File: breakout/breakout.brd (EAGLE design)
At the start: 30 x 26.8 mm, 34 parts, among them X1 PCIE-MINI-CONN

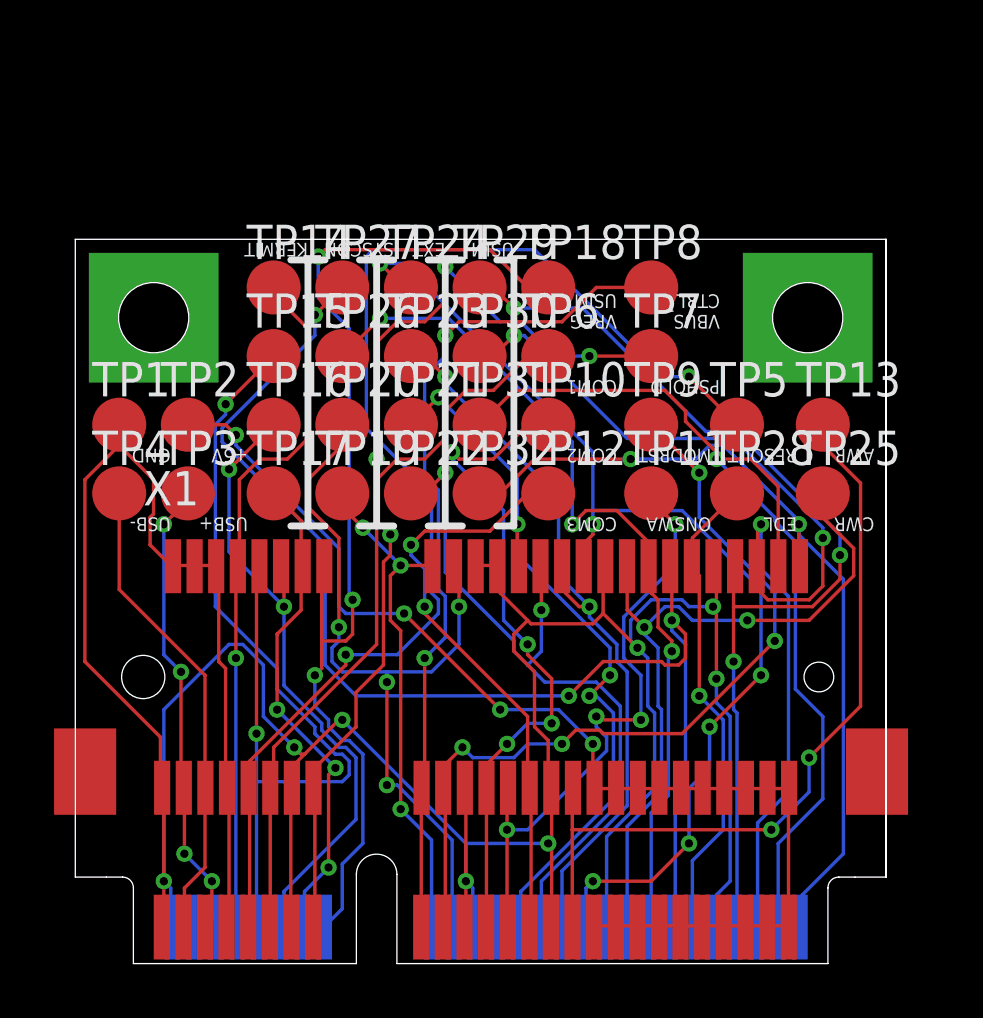
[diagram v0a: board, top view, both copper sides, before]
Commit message: Better routing of the +5V pins to handle large currents
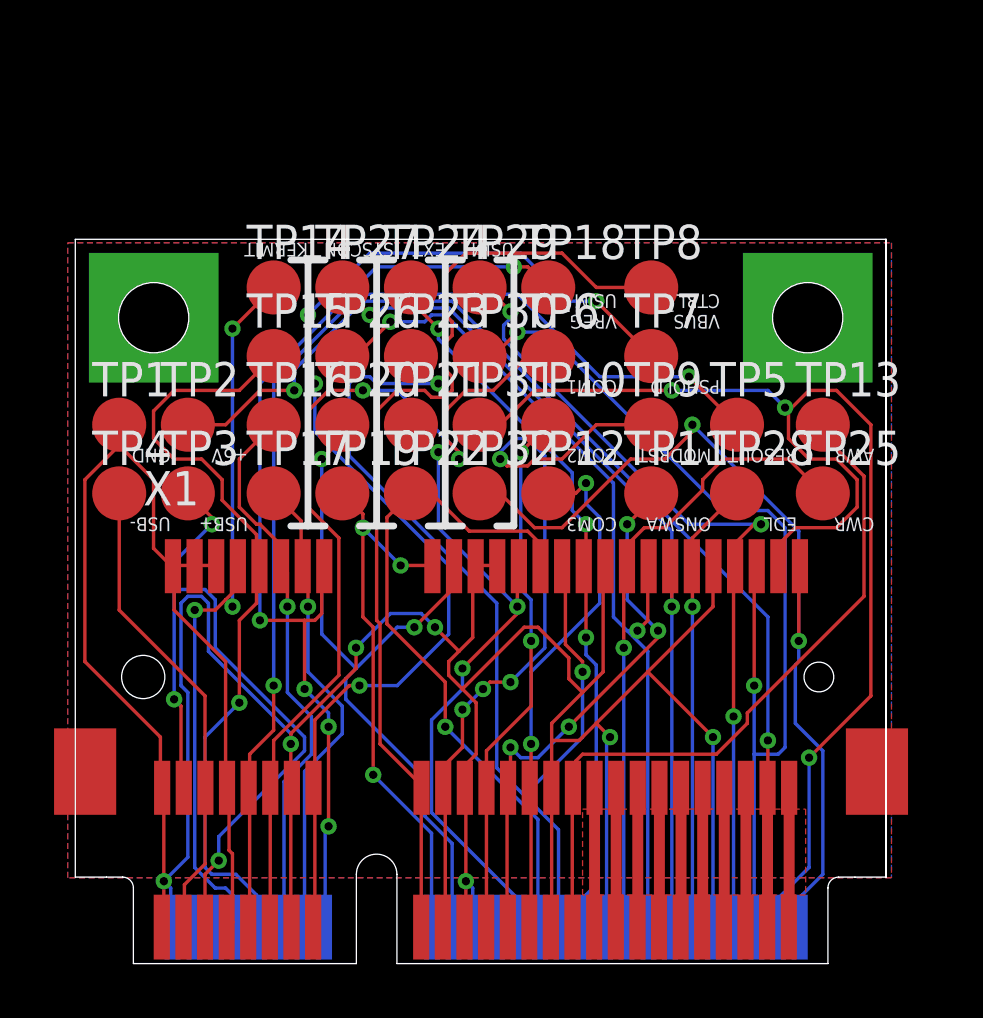
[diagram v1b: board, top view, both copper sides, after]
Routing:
- net +5V: track 43.0 -> 91.2 mm, vias 4 -> 2
- net UART_SYSCON_CTS: track 47.3 -> 32.3 mm, vias 3 -> 2
- net UART_EXT_RFR: track 40.6 -> 26.8 mm, vias 6 -> 3
- net USB_D-: track 17.3 -> 28.7 mm, vias 4 -> 3
- net UART_EXT_CTS: track 27.9 -> 38.0 mm
- net USIM_RESET_CONN: track 36.0 -> 45.7 mm, vias 1 -> 3
- net GPIO_COM1: track 27.0 -> 34.4 mm, vias 0 -> 2
- net GND: track 139.5 -> 146.8 mm, vias 8 -> 7
- net UART_KERMIT_CTS: track 35.6 -> 28.8 mm, vias 2 -> 1
- net PSHOLD: track 36.5 -> 43.2 mm
- net USIM_CLK_CONN: track 36.6 -> 30.5 mm
- net RESOUT: track 46.5 -> 41.1 mm
- net GPIO_COM2: track 24.8 -> 19.9 mm, vias 4 -> 2
- net VBUS_CTRL: track 31.2 -> 36.2 mm, vias 2 -> 0
- net CWR: track 26.9 -> 23.6 mm, vias 2 -> 1
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- added copper zone on layer 1, net +5V
- added copper zone on layer 1, net GND
- added copper zone on layer 16, net GND

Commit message: Fix incorrect signal in breakout board
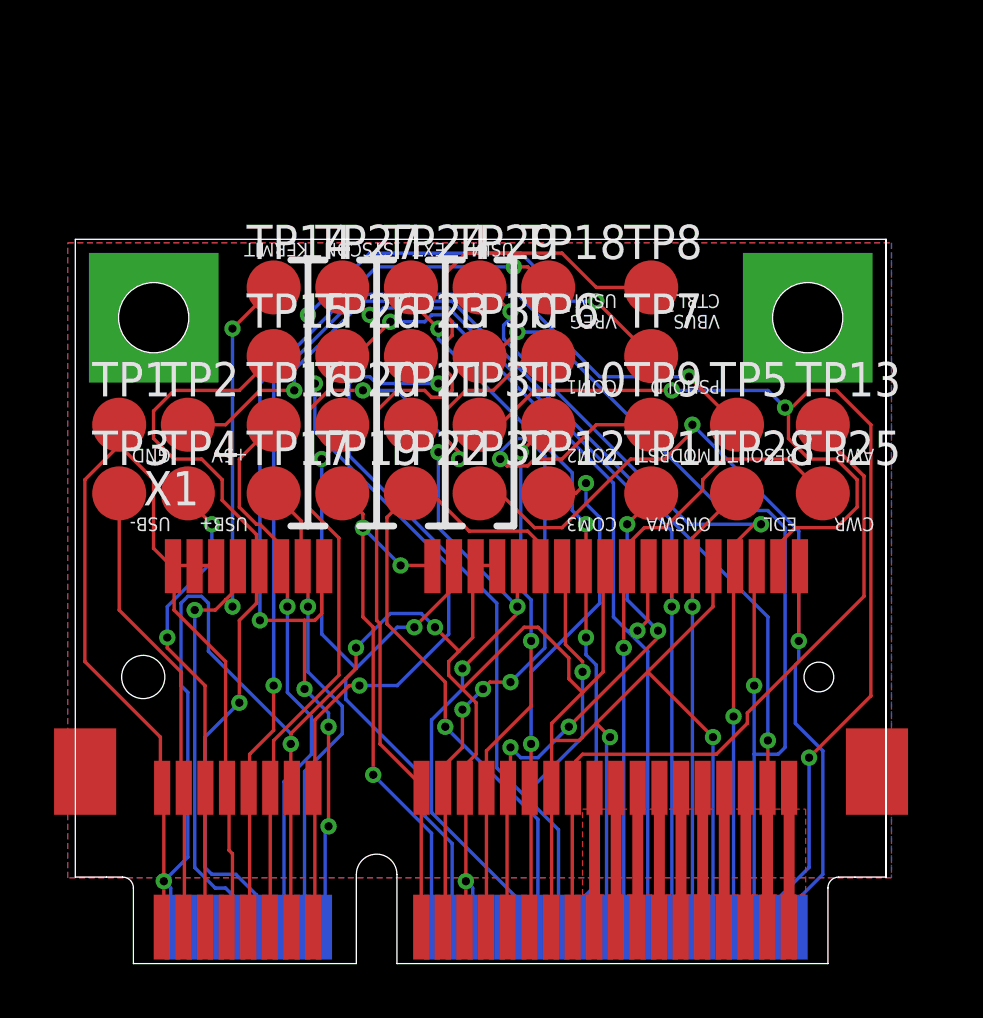
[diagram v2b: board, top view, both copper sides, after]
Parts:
- moved TP3 2.54 mm to (8.26, 22.5)
- moved TP4 2.54 mm to (10.8, 22.5)
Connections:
- removed net USB_D+: TP4.TP, U$1.3, X1.5
- removed net USB_D-: TP3.TP, U$1.5, X1.3
- new net USB_N: TP3.TP, U$1.3, X1.3
- new net USB_P: TP4.TP, U$1.5, X1.5
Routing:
- net USB_D-: track 28.7 -> 0.00 mm, vias 3 -> 0
- net USB_D+: track 17.7 -> 0.00 mm
- net USB_P: track 0.00 -> 17.7 mm, vias 0 -> 2
- net USB_N: track 0.00 -> 17.1 mm
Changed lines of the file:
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@@
 <layer number="21" name="tPlace" color="7" fill="1" visible="yes" active="yes"/>
 <layer number="22" name="bPlace" color="7" fill="1" visible="yes" active="yes"/>
-<layer number="23" name="tOrigins" color="15" fill="1" visible="no" active="yes"/>
-<layer number="24" name="bOrigins" color="15" fill="1" visible="no" active="yes"/>
-<layer number="25" name="tNames" color="7" fill="1" visible="no" active="yes"/>
-<layer number="26" name="bNames" color="7" fill="1" visible="no" active="yes"/>
-<layer number="27" name="tValues" color="7" fill="1" visible="no" active="yes"/>
-<layer number="28" name="bValues" color="7" fill="1" visible="no" active="yes"/>
+<layer number="23" name="tOrigins" color="15" fill="1" visible="yes" active="yes"/>
+<layer number="24" name="bOrigins" color="15" fill="1" visible="yes" active="yes"/>
+<layer number="25" name="tNames" color="7" fill="1" visible="yes" active="yes"/>
+<layer number="26" name="bNames" color="7" fill="1" visible="yes" active="yes"/>
+<layer number="27" name="tValues" color="7" fill="1" visible="yes" active="yes"/>
+<layer number="28" name="bValues" color="7" fill="1" visible="yes" active="yes"/>
 <layer number="29" name="tStop" color="7" fill="3" visible="no" active="yes"/>
 <layer number="30" name="bStop" color="7" fill="6" visible="no" active="yes"/>
@@
 <layer number="35" name="tGlue" color="7" fill="4" visible="no" active="yes"/>
 <layer number="36" name="bGlue" color="7" fill="5" visible="no" active="yes"/>
-<layer number="37" name="tTest" color="7" fill="1" visible="yes" active="yes"/>
-<layer number="38" name="bTest" color="7" fill="1" visible="yes" active="yes"/>
-<layer number="39" name="tKeepout" color="4" fill="11" visible="yes" active="yes"/>
-<layer number="40" name="bKeepout" color="1" fill="11" visible="yes" active="yes"/>
-<layer number="41" name="tRestrict" color="4" fill="10" visible="yes" active="yes"/>
-<layer number="42" name="bRestrict" color="1" fill="10" visible="yes" active="yes"/>
-<layer number="43" name="vRestrict" color="2" fill="10" visible="yes" active="yes"/>
+<layer number="37" name="tTest" color="7" fill="1" visible="no" active="yes"/>
+<layer number="38" name="bTest" color="7" fill="1" visible="no" active="yes"/>
+<layer number="39" name="tKeepout" color="4" fill="11" visible="no" active="yes"/>
+<layer number="40" name="bKeepout" color="1" fill="11" visible="no" active="yes"/>
+<layer number="41" name="tRestrict" color="4" fill="10" visible="no" active="yes"/>
+<layer number="42" name="bRestrict" color="1" fill="10" visible="no" active="yes"/>
+<layer number="43" name="vRestrict" color="2" fill="10" visible="no" active="yes"/>
 <layer number="44" name="Drills" color="7" fill="1" visible="yes" active="yes"/>
 <layer number="45" name="Holes" color="7" fill="1" visible="yes" active="yes"/>
@@
 </autorouter>
 <elements>
-<element name="TP3" library="testpad" package="TP20R" value="TPTP20R" x="10.795" y="22.479">
-<attribute name="TP_SIGNAL_NAME" value="" x="10.795" y="22.479" size="1.778" layer="27" display="off"/>
+<element name="TP3" library="testpad" package="TP20R" value="TPTP20R" x="8.255" y="22.479">
+<attribute name="TP_SIGNAL_NAME" value="" x="8.255" y="22.479" size="1.778" layer="27" display="off"/>
 </element>
 <element name="TP11" library="testpad" package="TP20R" value="TPTP20R" x="27.94" y="22.479">
@@
 <attribute name="TP_SIGNAL_NAME" value="" x="24.13" y="30.099" size="1.778" layer="27" display="off"/>
 </element>
-<element name="TP4" library="testpad" package="TP20R" value="TPTP20R" x="8.255" y="22.479">
-<attribute name="TP_SIGNAL_NAME" value="" x="8.255" y="22.479" size="1.778" layer="27" display="off"/>
+<element name="TP4" library="testpad" package="TP20R" value="TPTP20R" x="10.795" y="22.479">
+<attribute name="TP_SIGNAL_NAME" value="" x="10.795" y="22.479" size="1.778" layer="27" display="off"/>
 </element>
 <element name="TP19" library="testpad" package="TP20R" value="TPTP20R" x="16.51" y="22.479">
@@
 </elements>
 <signals>
-<signal name="USB_D-">
-<contactref element="X1" pad="3"/>
+<signal name="USB_P">
+<contactref element="X1" pad="5"/>
+<contactref element="TP4" pad="TP"/>
 <contactref element="U$1" pad="5"/>
-<contactref element="TP3" pad="TP"/>
-<wire x1="10.541" y1="14.605" x2="10.541" y2="11.684" width="0.127" layer="1"/>
-<wire x1="10.287" y1="14.859" x2="10.541" y2="14.605" width="0.127" layer="1"/>
-<wire x1="10.287" y1="19.939" x2="10.287" y2="18.923" width="0.127" layer="16"/>
-<wire x1="10.287" y1="18.923" x2="10.287" y2="14.859" width="0.127" layer="16"/>
-<wire x1="11.684" y1="21.336" x2="10.287" y2="19.939" width="0.127" layer="16"/>
-<wire x1="11.684" y1="21.59" x2="11.684" y2="21.336" width="0.127" layer="1"/>
-<wire x1="10.795" y1="22.479" x2="11.684" y2="21.59" width="0.127" layer="1"/>
-<wire x1="10.541" y1="11.684" x2="10.644" y2="11.5845" width="0.127" layer="1"/>
-<wire x1="11.43" y1="8.382" x2="11.43" y2="6.43" width="0.127" layer="1"/>
-<wire x1="11.938" y1="8.89" x2="11.43" y2="8.382" width="0.127" layer="1"/>
-<wire x1="11.938" y1="9.779" x2="11.938" y2="8.89" width="0.127" layer="16"/>
-<wire x1="15.113" y1="12.954" x2="11.938" y2="9.779" width="0.127" layer="16"/>
-<wire x1="15.113" y1="13.462" x2="15.113" y2="12.954" width="0.127" layer="16"/>
-<wire x1="11.811" y1="16.764" x2="15.113" y2="13.462" width="0.127" layer="16"/>
-<wire x1="11.811" y1="18.542" x2="11.811" y2="16.764" width="0.127" layer="16"/>
-<wire x1="11.43" y1="18.923" x2="11.811" y2="18.542" width="0.127" layer="16"/>
-<wire x1="10.287" y1="18.923" x2="11.43" y2="18.923" width="0.127" layer="16"/>
-<via x="10.287" y="14.859" extent="1-16" drill="0.3048"/>
+<wire x1="11.43" y1="6.43" x2="11.43" y2="11.557" width="0.127" layer="1"/>
+<wire x1="11.43" y1="11.557" x2="11.444" y2="11.5845" width="0.127" layer="1"/>
+<wire x1="10.795" y1="22.225" x2="10.795" y2="22.479" width="0.127" layer="1"/>
+<wire x1="11.684" y1="21.336" x2="10.795" y2="22.225" width="0.127" layer="1"/>
+<wire x1="11.684" y1="19.939" x2="11.684" y2="21.336" width="0.127" layer="16"/>
+<wire x1="10.033" y1="18.288" x2="11.684" y2="19.939" width="0.127" layer="16"/>
+<wire x1="10.033" y1="17.145" x2="10.033" y2="18.288" width="0.127" layer="16"/>
+<wire x1="10.033" y1="16.764" x2="10.033" y2="17.145" width="0.127" layer="1"/>
+<wire x1="11.43" y1="15.367" x2="10.033" y2="16.764" width="0.127" layer="1"/>
+<wire x1="11.43" y1="11.684" x2="11.43" y2="15.367" width="0.127" layer="1"/>
+<wire x1="11.43" y1="11.684" x2="11.444" y2="11.5845" width="0.127" layer="1"/>
 <via x="11.684" y="21.336" extent="1-16" drill="0.3048"/>
-<via x="11.938" y="8.89" extent="1-16" drill="0.3048"/>
-</signal>
-<signal name="USB_D+">
-<contactref element="X1" pad="5"/>
-<contactref element="U$1" pad="3"/>
-<contactref element="TP4" pad="TP"/>
-<wire x1="11.43" y1="8.763" x2="11.43" y2="11.557" width="0.127" layer="1"/>
-<wire x1="10.668" y1="8.001" x2="11.43" y2="8.763" width="0.127" layer="1"/>
-<wire x1="10.668" y1="6.477" x2="10.668" y2="8.001" width="0.127" layer="1"/>
-<wire x1="11.43" y1="11.557" x2="11.444" y2="11.5845" width="0.127" layer="1"/>
-<wire x1="10.668" y1="6.477" x2="10.63" y2="6.43" width="0.127" layer="1"/>
-<wire x1="8.255" y1="18.161" x2="8.255" y2="22.479" width="0.127" layer="1"/>
-<wire x1="11.43" y1="14.986" x2="8.255" y2="18.161" width="0.127" layer="1"/>
-<wire x1="11.43" y1="11.684" x2="11.43" y2="14.986" width="0.127" layer="1"/>
-<wire x1="11.43" y1="11.684" x2="11.444" y2="11.5845" width="0.127" layer="1"/>
+<via x="10.033" y="17.145" extent="1-16" drill="0.3048"/>
 </signal>
 <signal name="RESOUT">
@@
 <wire x1="11.811" y1="6.477" x2="11.83" y2="6.43" width="0.127" layer="16"/>
 <wire x1="11.049" y1="6.477" x2="11.03" y2="6.43" width="0.127" layer="16"/>
-<contactref element="U$1" pad="GND@1"/>
-<contactref element="U$1" pad="GND@2"/>
 <wire x1="22.225" y1="6.477" x2="21.463" y2="6.477" width="0.127" layer="16"/>
 <wire x1="21.463" y1="6.477" x2="21.43" y2="6.43" width="0.127" layer="16"/>
@@
 <vertex x="6.35" y="8.255"/>
 </polygon>
-<wire x1="30.244" y1="19.7845" x2="33.73" y2="28.98" width="0" layer="19" extent="1-1"/>
+<contactref element="U$1" pad="GND@1"/>
+<contactref element="U$1" pad="GND@2"/>
+<wire x1="33.73" y1="28.98" x2="30.244" y2="19.7845" width="0" layer="19" extent="1-1"/>
+</signal>
+<signal name="USB_N">
+<contactref element="X1" pad="3"/>
+<contactref element="TP3" pad="TP"/>
+<contactref element="U$1" pad="3"/>
+<wire x1="10.668" y1="6.477" x2="10.668" y2="11.557" width="0.127" layer="1"/>
+<wire x1="10.668" y1="11.557" x2="10.644" y2="11.5845" width="0.127" layer="1"/>
+<wire x1="10.668" y1="6.477" x2="10.63" y2="6.43" width="0.127" layer="1"/>
+<wire x1="8.255" y1="18.161" x2="8.255" y2="22.479" width="0.127" layer="1"/>
+<wire x1="10.541" y1="15.875" x2="8.255" y2="18.161" width="0.127" layer="1"/>
+<wire x1="10.541" y1="11.684" x2="10.541" y2="15.875" width="0.127" layer="1"/>
+<wire x1="10.541" y1="11.684" x2="10.644" y2="11.5845" width="0.127" layer="1"/>
 </signal>
 </signals>

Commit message: Updated board to be right size
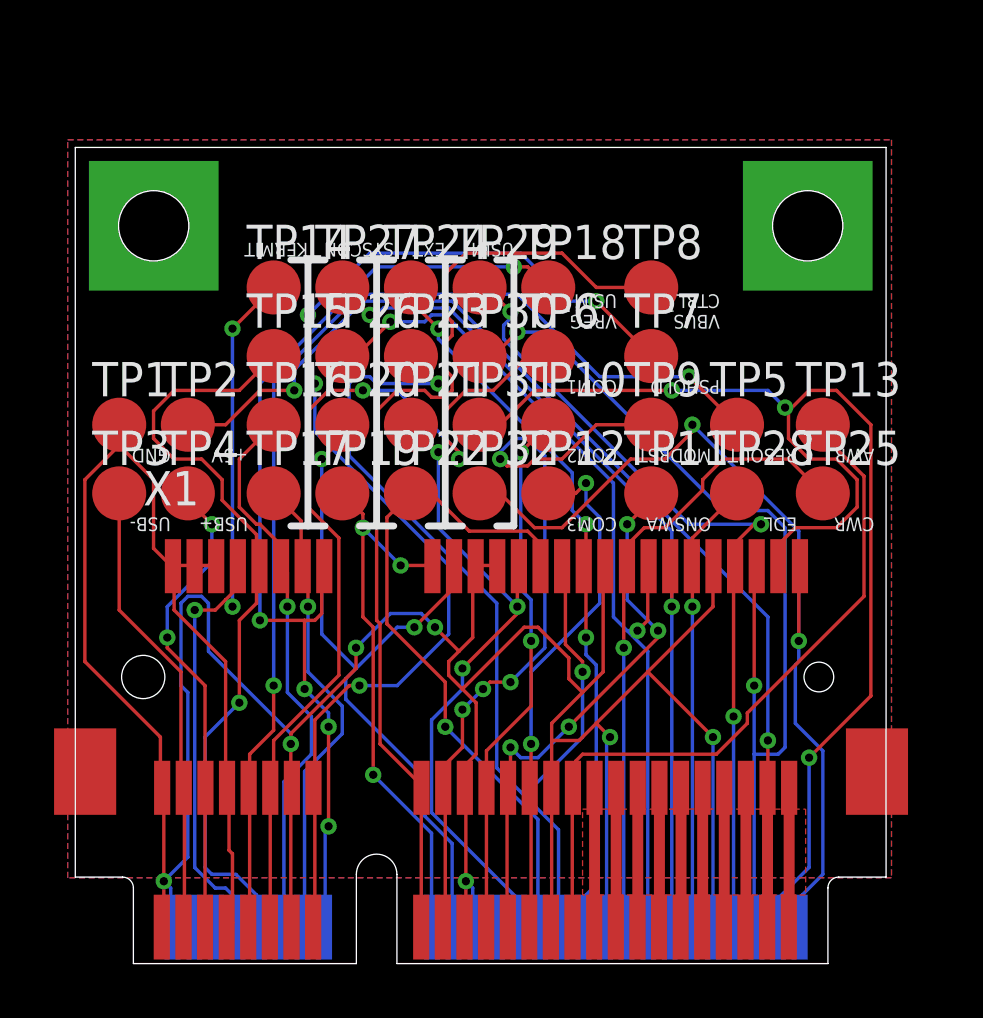
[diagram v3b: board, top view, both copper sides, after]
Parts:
- U$1: device mini-pci-e:HALF-MINI-PCI-E -> mini-pci-e:VITA-MINI-PCI-E
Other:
- board size 30 x 26.8 mm -> 30 x 30.2 mm
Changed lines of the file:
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@@
 <attribute name="TP_SIGNAL_NAME" value="" x="24.13" y="25.019" size="1.778" layer="27" display="off"/>
 </element>
-<element name="U$1" library="mini-pci-e" package="HALF-MINI-PCI-E" value="VITA-CUSTOM" x="17.78" y="5.08"/>
+<element name="U$1" library="mini-pci-e" package="VITA-MINI-PCI-E" value="VITA-CUSTOM" x="17.78" y="5.08"/>
 <element name="X1" library="con-molex" package="PCIE-MINI-CONN" value="PCIE-MINI-CONN" x="9.144" y="15.6845"/>
 </elements>
@@
 <wire x1="30.226" y1="6.477" x2="30.23" y2="6.43" width="0.127" layer="16"/>
 <polygon width="0.4064" layer="1" rank="2">
-<vertex x="6.35" y="31.75"/>
-<vertex x="36.83" y="31.75"/>
+<vertex x="6.35" y="35.56"/>
+<vertex x="36.83" y="35.56"/>
 <vertex x="36.83" y="8.255"/>
 <vertex x="6.35" y="8.255"/>
 </polygon>
 <polygon width="0.4064" layer="16">
-<vertex x="6.35" y="31.75"/>
-<vertex x="36.83" y="31.75"/>
-<vertex x="36.83" y="31.115"/>
+<vertex x="6.35" y="35.56"/>
+<vertex x="36.83" y="35.56"/>
 <vertex x="36.83" y="8.255"/>
 <vertex x="6.35" y="8.255"/>
@@
 <contactref element="U$1" pad="GND@1"/>
 <contactref element="U$1" pad="GND@2"/>
-<wire x1="33.73" y1="28.98" x2="30.244" y2="19.7845" width="0" layer="19" extent="1-1"/>
 </signal>
 <signal name="USB_N">
